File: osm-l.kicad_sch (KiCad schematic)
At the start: 51 parts, among them SW1 SW_KMR211NGLFS_SMD, SW2 SW_KMR211NGLFS_SMD, SW3 SW_KMR211NGLFS_SMD, U1 OSM-L_Carrier-side, U2 74AUP2G132, U3 74AUP2G132

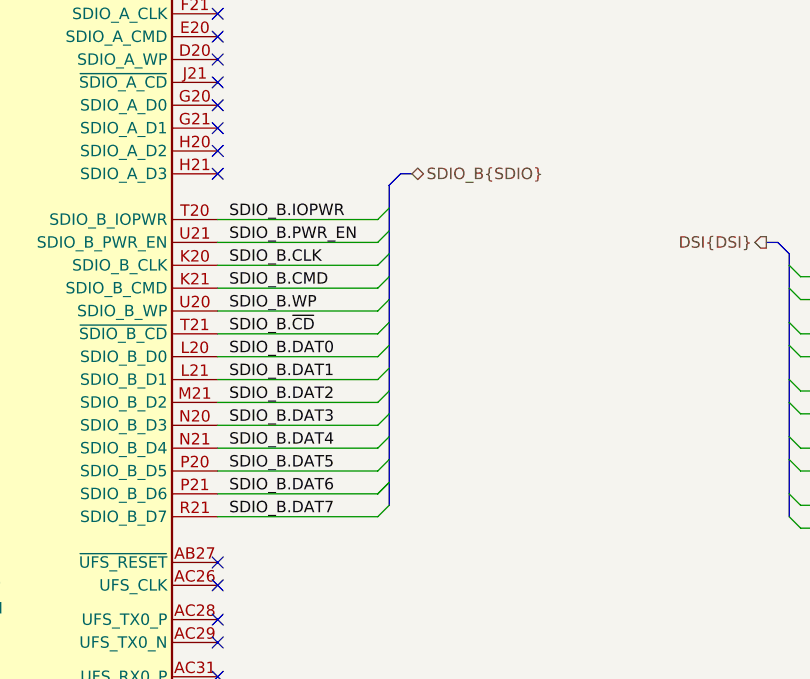
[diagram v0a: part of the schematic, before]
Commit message: [#83767] Fix SDIO net class assignment, synchronize PCB with schematic
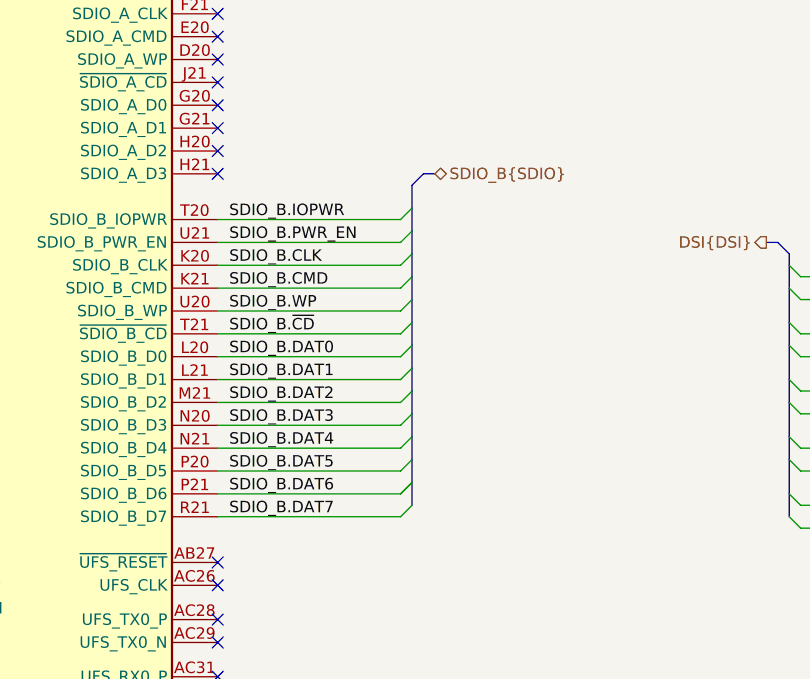
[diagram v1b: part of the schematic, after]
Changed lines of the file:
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@@
 	)
 	(bus_entry
-		(at 379.73 325.12)
+		(at 382.27 325.12)
 		(size -1.27 1.27)
 		(stroke
@@
 	)
 	(bus_entry
-		(at 379.73 317.5)
+		(at 382.27 317.5)
 		(size -1.27 1.27)
 		(stroke
@@
 	)
 	(bus_entry
-		(at 379.73 342.9)
+		(at 382.27 342.9)
 		(size -1.27 1.27)
 		(stroke
@@
 	)
 	(bus_entry
-		(at 379.73 322.58)
+		(at 382.27 322.58)
 		(size -1.27 1.27)
 		(stroke
@@
 	)
 	(bus_entry
-		(at 379.73 335.28)
+		(at 382.27 335.28)
 		(size -1.27 1.27)
 		(stroke
@@
 	)
 	(bus_entry
-		(at 379.73 327.66)
+		(at 382.27 327.66)
 		(size -1.27 1.27)
 		(stroke
@@
 	)
 	(bus_entry
-		(at 379.73 342.9)
+		(at 382.27 342.9)
 		(size -1.27 1.27)
 		(stroke
@@
 	)
 	(bus_entry
-		(at 379.73 312.42)
+		(at 382.27 312.42)
 		(size -1.27 1.27)
 		(stroke
@@
 	)
 	(bus_entry
-		(at 379.73 314.96)
+		(at 382.27 314.96)
 		(size -1.27 1.27)
 		(stroke
@@
 	)
 	(bus_entry
-		(at 379.73 340.36)
+		(at 382.27 340.36)
 		(size -1.27 1.27)
 		(stroke
@@
 	)
 	(bus_entry
-		(at 379.73 330.2)
+		(at 382.27 330.2)
 		(size -1.27 1.27)
 		(stroke
@@
 	)
 	(bus_entry
-		(at 379.73 337.82)
+		(at 382.27 337.82)
 		(size -1.27 1.27)
 		(stroke
@@
 	)
 	(bus_entry
-		(at 379.73 320.04)
+		(at 382.27 320.04)
 		(size -1.27 1.27)
 		(stroke
@@
 	)
 	(bus_entry
-		(at 379.73 345.44)
+		(at 382.27 345.44)
 		(size -1.27 1.27)
 		(stroke
@@
 	)
 	(bus_entry
-		(at 379.73 332.74)
+		(at 382.27 332.74)
 		(size -1.27 1.27)
 		(stroke
@@
 	(wire
 		(pts
-			(xy 360.68 316.23) (xy 378.46 316.23)
+			(xy 360.68 316.23) (xy 381 316.23)
 		)
 		(stroke
@@
 	(bus
 		(pts
-			(xy 379.73 342.9) (xy 379.73 345.44)
+			(xy 382.27 342.9) (xy 382.27 345.44)
 		)
 		(stroke
@@
 	(wire
 		(pts
-			(xy 360.68 321.31) (xy 378.46 321.31)
+			(xy 360.68 321.31) (xy 381 321.31)
 		)
 		(stroke
@@
 	(bus
 		(pts
-			(xy 379.73 337.82) (xy 379.73 340.36)
+			(xy 382.27 337.82) (xy 382.27 340.36)
 		)
 		(stroke
@@
 	(bus
 		(pts
-			(xy 382.27 308.61) (xy 381 308.61)
+			(xy 384.81 308.61) (xy 383.54 308.61)
 		)
 		(stroke
@@
 	(bus
 		(pts
-			(xy 379.73 332.74) (xy 379.73 335.28)
+			(xy 382.27 332.74) (xy 382.27 335.28)
 		)
 		(stroke
@@
 	(wire
 		(pts
-			(xy 360.68 323.85) (xy 378.46 323.85)
+			(xy 360.68 323.85) (xy 381 323.85)
 		)
 		(stroke
@@
 	(bus
 		(pts
-			(xy 379.73 309.88) (xy 381 308.61)
+			(xy 382.27 309.88) (xy 383.54 308.61)
 		)
 		(stroke
@@
 	(wire
 		(pts
-			(xy 360.68 328.93) (xy 378.46 328.93)
+			(xy 360.68 328.93) (xy 381 328.93)
 		)
 		(stroke
@@
 	(wire
 		(pts
-			(xy 360.68 326.39) (xy 378.46 326.39)
+			(xy 360.68 326.39) (xy 381 326.39)
 		)
 		(stroke
@@
 	(wire
 		(pts
-			(xy 360.68 318.77) (xy 378.46 318.77)
+			(xy 360.68 318.77) (xy 381 318.77)
 		)
 		(stroke
@@
 	(bus
 		(pts
-			(xy 379.73 330.2) (xy 379.73 332.74)
+			(xy 382.27 330.2) (xy 382.27 332.74)
 		)
 		(stroke
@@
 	(bus
 		(pts
-			(xy 379.73 340.36) (xy 379.73 342.9)
+			(xy 382.27 340.36) (xy 382.27 342.9)
 		)
 		(stroke
@@
 	(bus
 		(pts
-			(xy 379.73 322.58) (xy 379.73 325.12)
+			(xy 382.27 322.58) (xy 382.27 325.12)
 		)
 		(stroke
@@
 	(wire
 		(pts
-			(xy 360.68 334.01) (xy 378.46 334.01)
+			(xy 360.68 334.01) (xy 381 334.01)
 		)
 		(stroke
@@
 	(bus
 		(pts
-			(xy 379.73 325.12) (xy 379.73 327.66)
+			(xy 382.27 325.12) (xy 382.27 327.66)
 		)
 		(stroke
@@
 	(bus
 		(pts
-			(xy 379.73 335.28) (xy 379.73 337.82)
+			(xy 382.27 335.28) (xy 382.27 337.82)
 		)
 		(stroke
@@
 	(bus
 		(pts
-			(xy 379.73 327.66) (xy 379.73 330.2)
+			(xy 382.27 327.66) (xy 382.27 330.2)
 		)
 		(stroke
@@
 	(bus
 		(pts
-			(xy 379.73 314.96) (xy 379.73 317.5)
+			(xy 382.27 314.96) (xy 382.27 317.5)
 		)
 		(stroke
@@
 	(wire
 		(pts
-			(xy 360.68 339.09) (xy 378.46 339.09)
+			(xy 360.68 339.09) (xy 381 339.09)
 		)
 		(stroke
@@
 	(wire
 		(pts
-			(xy 360.68 313.69) (xy 378.46 313.69)
+			(xy 360.68 313.69) (xy 381 313.69)
 		)
 		(stroke
@@
 	(wire
 		(pts
-			(xy 360.68 341.63) (xy 378.46 341.63)
+			(xy 360.68 341.63) (xy 381 341.63)
 		)
 		(stroke
@@
 	(wire
 		(pts
-			(xy 360.68 346.71) (xy 378.46 346.71)
+			(xy 360.68 346.71) (xy 381 346.71)
 		)
 		(stroke
@@
 	(bus
 		(pts
-			(xy 379.73 309.88) (xy 379.73 312.42)
+			(xy 382.27 309.88) (xy 382.27 312.42)
 		)
 		(stroke
@@
 	(bus
 		(pts
-			(xy 379.73 317.5) (xy 379.73 320.04)
+			(xy 382.27 317.5) (xy 382.27 320.04)
 		)
 		(stroke
@@
 	(bus
 		(pts
-			(xy 379.73 312.42) (xy 379.73 314.96)
+			(xy 382.27 312.42) (xy 382.27 314.96)
 		)
 		(stroke
@@
 	(bus
 		(pts
-			(xy 379.73 320.04) (xy 379.73 322.58)
+			(xy 382.27 320.04) (xy 382.27 322.58)
 		)
 		(stroke
@@
 	(wire
 		(pts
-			(xy 360.68 344.17) (xy 378.46 344.17)
+			(xy 360.68 344.17) (xy 381 344.17)
 		)
 		(stroke
@@
 	(wire
 		(pts
-			(xy 360.68 331.47) (xy 378.46 331.47)
+			(xy 360.68 331.47) (xy 381 331.47)
 		)
 		(stroke
@@
 	(wire
 		(pts
-			(xy 360.68 336.55) (xy 378.46 336.55)
+			(xy 360.68 336.55) (xy 381 336.55)
 		)
 		(stroke
@@
 	(hierarchical_label "SDIO_B{SDIO}"
 		(shape bidirectional)
-		(at 382.27 308.61 0)
+		(at 384.81 308.61 0)
 		(effects
 			(font
@@
 		(length 2.54)
 		(shape round)
-		(at 379.73 313.69 270)
+		(at 275.59 52.07 90)
 		(effects
 			(font
 				(size 1.27 1.27)
 			)
-			(justify right bottom)
+			(justify left bottom)
 		)
-		(property "Netclass" "50Ohm-se"
-			(at 383.54 313.69 0)
+		(property "Netclass" "90Ohm-diff"
+			(at 271.78 52.07 0)
 			(effects
 				(font
 					(size 1.27 1.27)
 				)
-				(justify left)
+				(justify right)
 			)
 		)
 		(property "Component Class" ""
-			(at 579.12 190.5 0)
+			(at 76.2 175.26 0)
 			(effects
 				(font
@@
 					(italic yes)
 				)
-				(justify left)
+				(justify right)
 			)
 		)
@@
 		(length 2.54)
 		(shape round)
-		(at 275.59 52.07 90)
+		(at 382.27 313.69 270)
 		(effects
 			(font
 				(size 1.27 1.27)
 			)
-			(justify left bottom)
+			(justify right bottom)
 		)
-		(property "Netclass" "90Ohm-diff"
-			(at 271.78 52.07 0)
+		(property "Netclass" "50Ohm-se"
+			(at 386.08 313.69 0)
 			(effects
 				(font
 					(size 1.27 1.27)
 				)
-				(justify right)
+				(justify left)
 			)
 		)
 		(property "Component Class" ""
-			(at 76.2 175.26 0)
+			(at 581.66 190.5 0)
 			(effects
 				(font
@@
 					(italic yes)
 				)
-				(justify right)
+				(justify left)
 			)
 		)

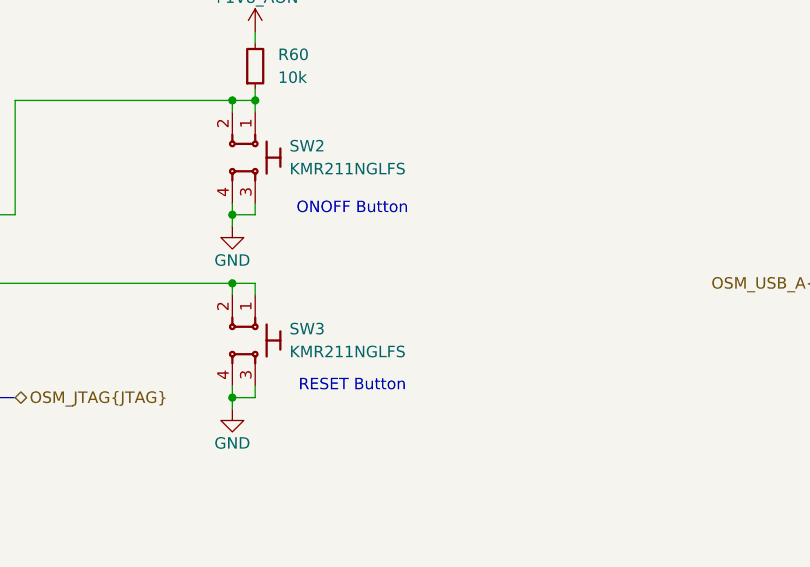
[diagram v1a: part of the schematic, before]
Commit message: [#83767] Add alternative reset signal
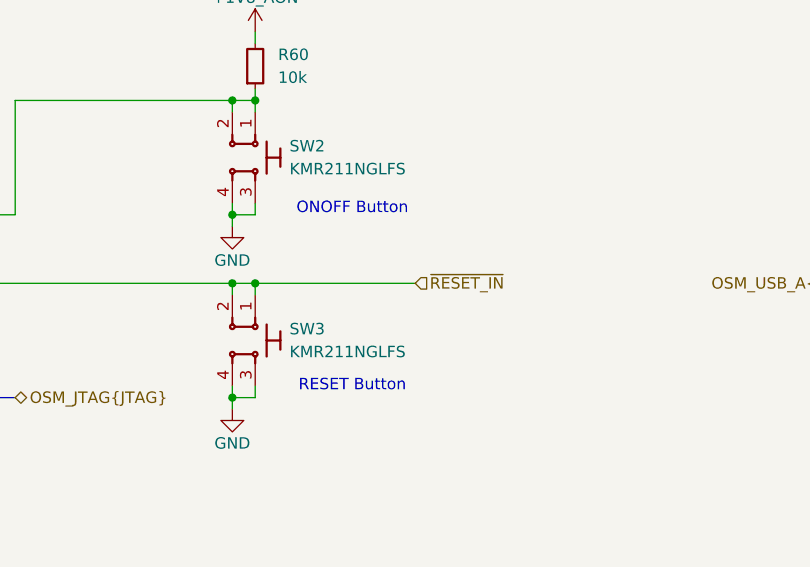
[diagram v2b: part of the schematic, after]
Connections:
- net ~{RESET_IN}: now reaches SW3.1, SW3.2, U1.U17 (~{RESET_IN})
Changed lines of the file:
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@@
 	)
 	(junction
+		(at 201.93 48.26)
+		(diameter 0)
+		(color 0 0 0 0)
+	)
+	(junction
 		(at 199.39 48.26)
 		(diameter 0)
@@
 	(wire
 		(pts
+			(xy 201.93 48.26) (xy 219.71 48.26)
+		)
+		(stroke
+			(width 0)
+			(type default)
+		)
+	)
+	(wire
+		(pts
 			(xy 95.25 107.95) (xy 95.25 114.3)
 		)
@@
 		)
 	)
+	(hierarchical_label "~{RESET_IN}"
+		(shape input)
+		(at 219.71 48.26 0)
+		(effects
+			(font
+				(size 1.27 1.27)
+			)
+			(justify left)
+		)
+	)

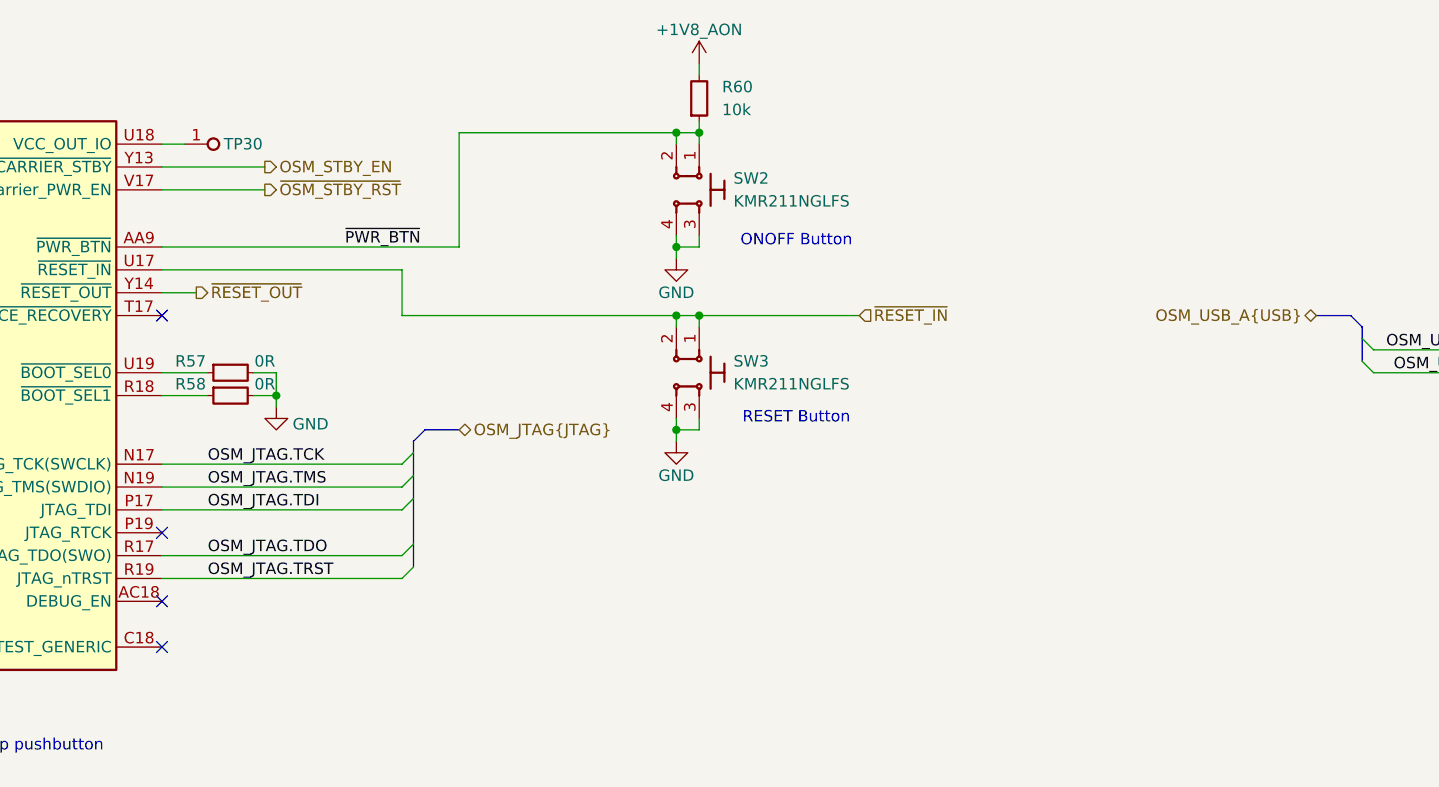
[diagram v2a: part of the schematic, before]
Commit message: [#83767] Add button debouncing
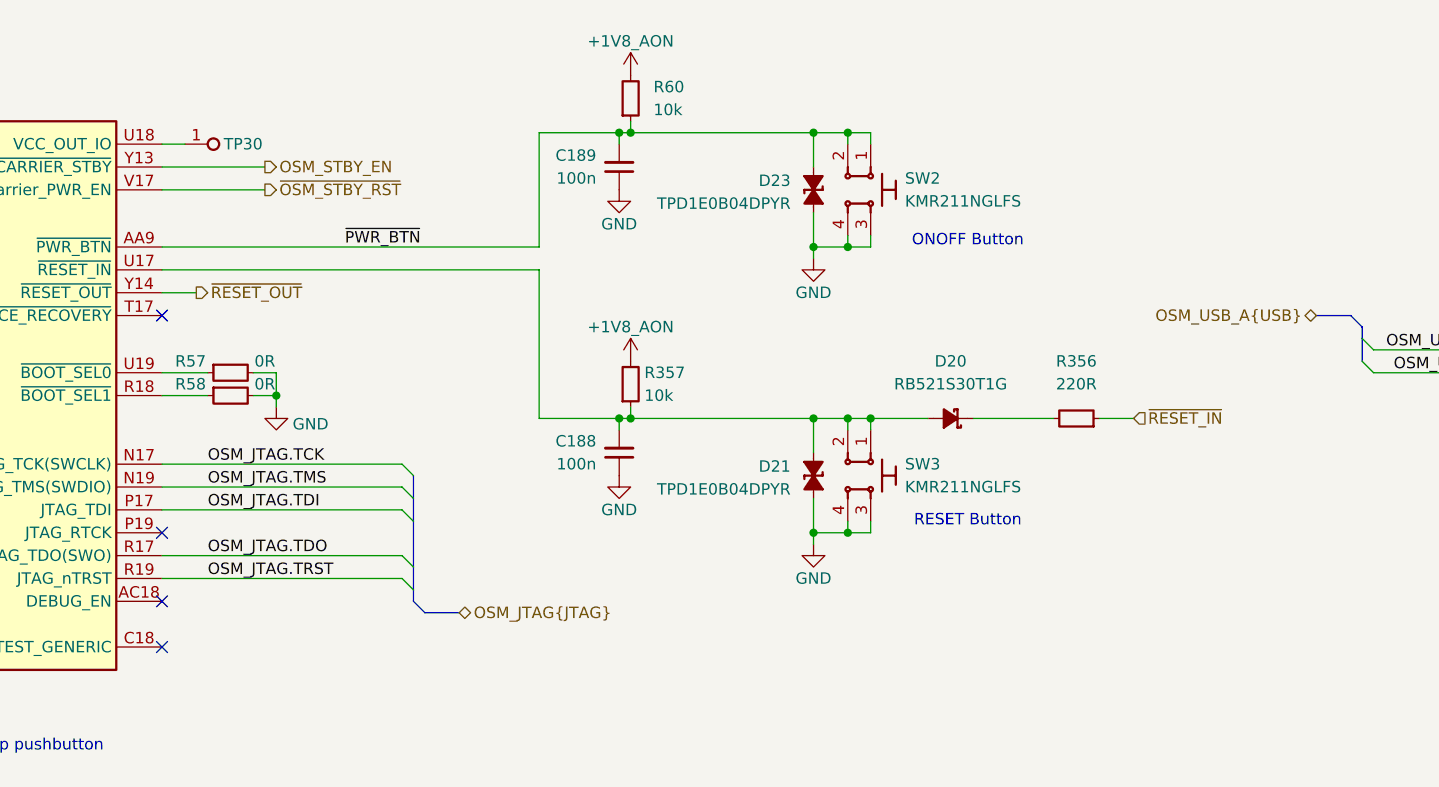
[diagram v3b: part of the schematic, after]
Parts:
- added C188, C189: C_100n_0402, antmicro-footprints:C_0402_1005Metric, symbol antmicroCapacitors0402:C_100n_0402
- added D20: RB521S30T1G, antmicro-footprints:SOD-523, symbol antmicroDiodesRectifiersSingle:RB521S30T1G
- added D21, D23: TPD1E0B04_XDFN-2, antmicro-footprints:XDFN-2_1x0.60mm, symbol antmicroTVSDiodes:TPD1E0B04_XDFN-2
- added R356: R_220R_0402, antmicro-footprints:R_0402_1005Metric, symbol antmicroResistors0402:R_220R_0402
- added R357: R_10k_0402, antmicro-footprints:R_0402_1005Metric, symbol antmicroResistors0402:R_10k_0402
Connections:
- net +1V8_AON: now also R357.2
- net GND: now also C188.1, C189.1, D21.1 (C), D23.1 (C)
- net ~{PWR_BTN}: now also C189.2, D23.2 (A)
- net ~{RESET_IN}: now also R356.1; no longer SW3.1, SW3.2, U1.U17 (~{RESET_IN})
- new net: D20.1 (C), R356.2
- new net: C188.2, D20.2 (A), D21.2 (A), R357.1, SW3.1, SW3.2, U1.U17 (~{RESET_IN})
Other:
- moved on the sheet: R60, SW2, SW3

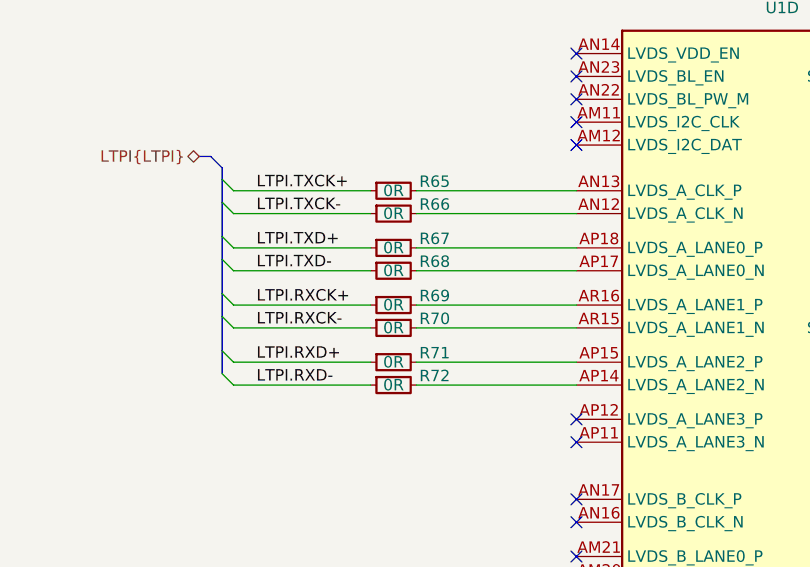
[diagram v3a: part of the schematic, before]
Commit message: [#83767] Remove redundant OSM 0R on LTPI
Bias circuitry can be used as path selection
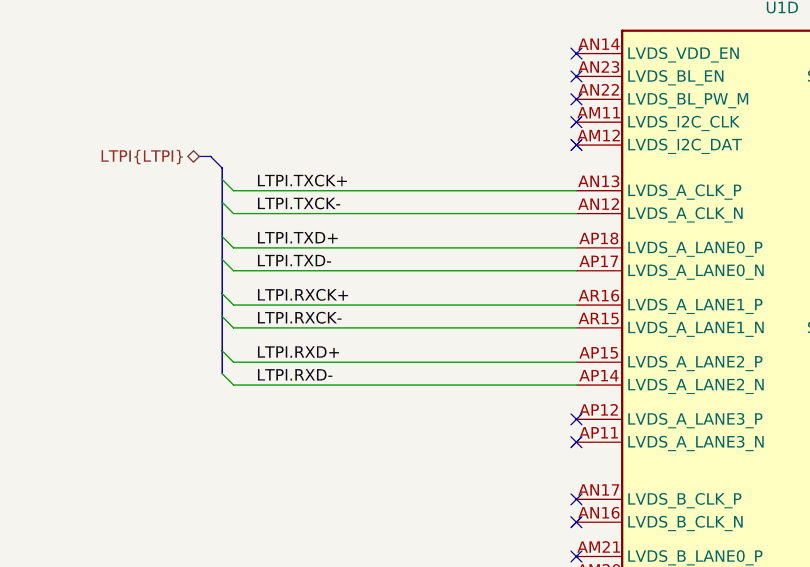
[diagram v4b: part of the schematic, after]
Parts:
- removed R65, R66, R67, R68, R69, R70, R71, R72: R_0R_0402, antmicro-footprints:R_0402_1005Metric, symbol antmicroResistors0402:R_0R_0402
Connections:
- net LTPI.RXCK+: now also U1.AR16 (LVDS_A_LANE1_P)
- net LTPI.RXCK-: now also U1.AR15 (LVDS_A_LANE1_N)
- net LTPI.RXD+: now also U1.AP15 (LVDS_A_LANE2_P)
- net LTPI.RXD-: now also U1.AP14 (LVDS_A_LANE2_N)
- net LTPI.TXCK+: now also U1.AN13 (LVDS_A_CLK_P)
- net LTPI.TXCK-: now also U1.AN12 (LVDS_A_CLK_N)
- net LTPI.TXD+: now also U1.AP18 (LVDS_A_LANE0_P)
- net LTPI.TXD-: now also U1.AP17 (LVDS_A_LANE0_N)

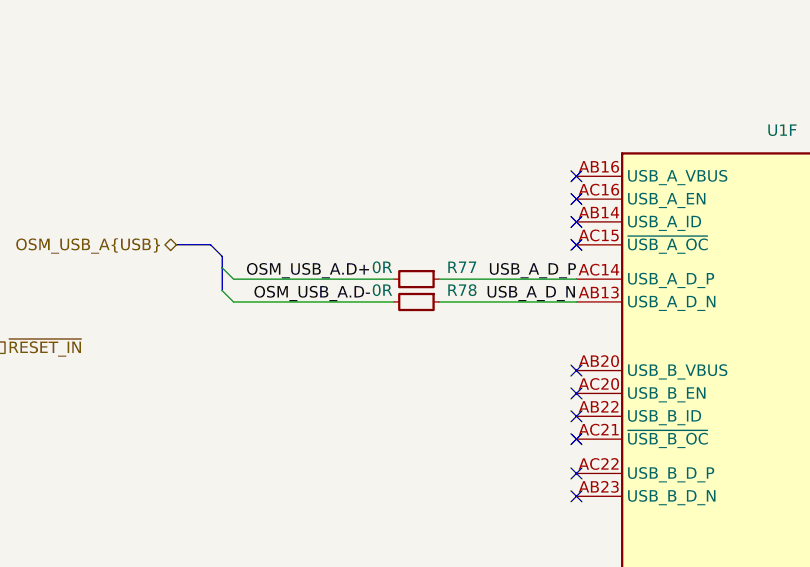
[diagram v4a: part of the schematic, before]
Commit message: [#83767] Remove redundant 0R on USB_A
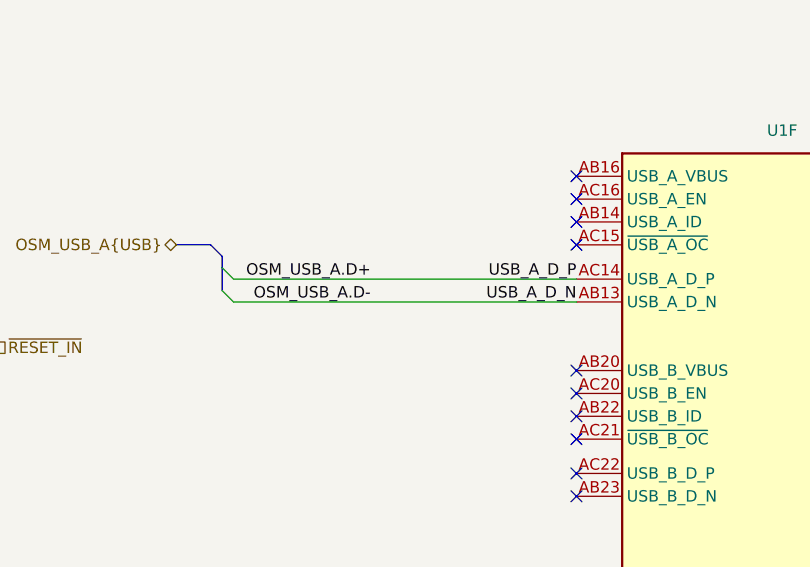
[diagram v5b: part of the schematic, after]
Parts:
- removed R77, R78: R_0R_0402, antmicro-footprints:R_0402_1005Metric, symbol antmicroResistors0402:R_0R_0402
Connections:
- net USB_A_D_N is gone; now on net OSM_USB_A.D-: U1.AB13 (USB_A_D_N)
- net USB_A_D_P is gone; now on net OSM_USB_A.D+: U1.AC14 (USB_A_D_P)
